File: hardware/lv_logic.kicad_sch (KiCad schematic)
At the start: 3 parts, among them IC2 CD4081BM96, IC3 CD40106BM96, IC4 CD4081BM96

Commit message: add enable timer in logic block
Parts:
- added C6: ??, symbol Device:C
- added Q4: NMOS, symbol Simulation_SPICE:NMOS
- added R6: ??, symbol Device:R_US
- added R8: 10k, symbol Device:R_US
- added U2: Inverter_Schmitt_Dual, symbol 74xGxx:Inverter_Schmitt_Dual
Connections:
- net +12V_LOGIC: now also R6.1, U2.5 (V_{CC})
- net +12V_SHDW: no longer IC2.13 (H)
- net ENABLE_IN: now also Q4.2 (G), R8.2; no longer IC2.12 (G), IC2.2 (B), IC4.1 (A)
- net GND: now also C6.2, Q4.3 (S), R8.1, U2.2 (GND), U2.3 (2A)
- new net: C6.1, Q4.1 (D), R6.2, U2.1 (1A)
- new net: IC2.12 (G), IC4.1 (A), U2.6 (1Y)
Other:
- note added: "Enable 50ms timer"
- moved on the sheet: IC2, IC3, IC4

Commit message: create hv_power hierarchical sheet; rename hi_sense ad hv_sense to meet project standards
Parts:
- removed U2: Inverter_Schmitt_Dual, symbol 74xGxx:Inverter_Schmitt_Dual
- added IC5: TC4S584F,LF, SOT-25, symbol Libary_Loader:TC4S584F,LF
- C6: value ?? -> 1uF
- R6: value ?? -> 55k
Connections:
- net +12V_LOGIC: now also C6.2, IC5.5 (VDD)
- net +12V_SHDW: now also IC2.13 (H)
- net GND: now also IC5.3 (VSS); no longer C6.2
- net at C6.1, Q4.1 (D), R6.2: now also IC5.2 (IN_A)
- net at IC2.12 (G), IC4.1 (A): now also IC2.2 (B), IC5.4 (OUT_~{X})

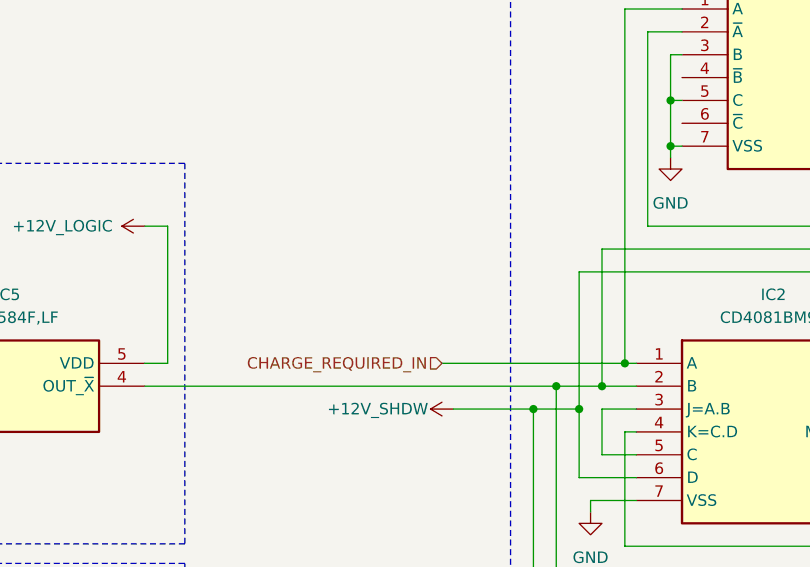
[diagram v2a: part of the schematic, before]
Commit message: refactor project layout merging high and low voltage in the same pcb
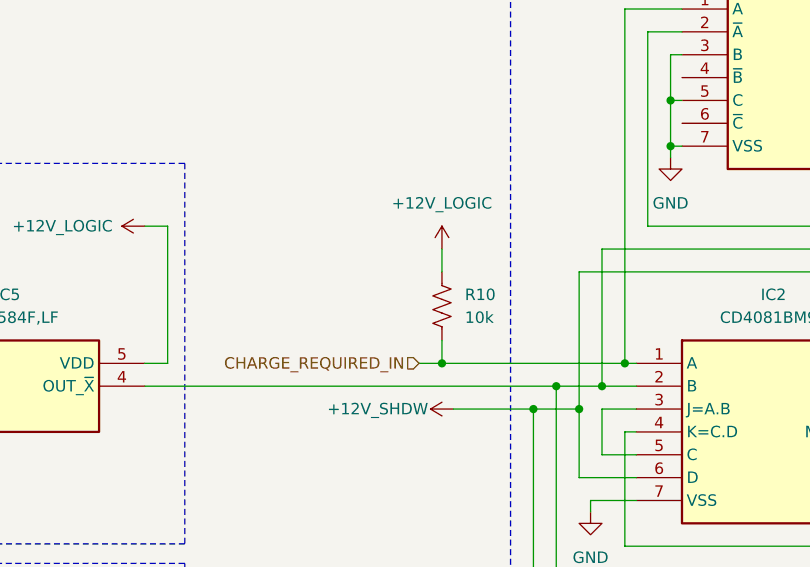
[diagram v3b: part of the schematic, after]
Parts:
- added R10: 10k, symbol Device:R_US
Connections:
- net +12V_LOGIC: now also R10.1
- net CHARGE_REQUIRED_IN: now also R10.2
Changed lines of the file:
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@@
+	)
+	(junction
+		(at 144.78 73.66)
+		(diameter 0)
+		(color 0 0 0 0)
 	)
 	(junction
@@
 	(wire
 		(pts
+			(xy 144.78 60.96) (xy 144.78 63.5)
+		)
+		(stroke
+			(width 0)
+			(type default)
+		)
+	)
+	(wire
+		(pts
 			(xy 171.45 36.83) (xy 167.64 36.83)
 		)
@@
 	(wire
 		(pts
+			(xy 144.78 71.12) (xy 144.78 73.66)
+		)
+		(stroke
+			(width 0)
+			(type default)
+		)
+	)
+	(wire
+		(pts
 			(xy 170.18 44.45) (xy 171.45 44.45)
 		)
@@
 	(wire
 		(pts
-			(xy 144.78 73.66) (xy 165.1 73.66)
-		)
-		(stroke
-			(width 0)
-			(type default)
-		)
-	)
-	(wire
-		(pts
 			(xy 196.85 76.2) (xy 214.63 76.2)
 		)
@@
 		(pts
 			(xy 111.76 73.66) (xy 114.3 73.66)
+		)
+		(stroke
+			(width 0)
+			(type default)
+		)
+	)
+	(wire
+		(pts
+			(xy 142.24 73.66) (xy 165.1 73.66)
 		)
 		(stroke
@@
 	(hierarchical_label "CHARGE_REQUIRED_IN"
 		(shape input)
-		(at 144.78 73.66 180)
+		(at 142.24 73.66 180)
 		(effects
 			(font
@@
 	)
 	(symbol
+		(lib_id "Device:R_US")
+		(at 144.78 67.31 0)
+		(unit 1)
+		(body_style 1)
+		(exclude_from_sim no)
+		(in_bom yes)
+		(on_board yes)
+		(in_pos_files yes)
+		(dnp no)
+		(fields_autoplaced yes)
+		(property "Reference" "R10"
+			(at 147.32 66.0399 0)
+			(show_name no)
+			(do_not_autoplace no)
+			(effects
+				(font
+					(size 1.27 1.27)
+				)
+				(justify left)
+			)
+		)
+		(property "Value" "10k"
+			(at 147.32 68.5799 0)
+			(show_name no)
+			(do_not_autoplace no)
+			(effects
+				(font
+					(size 1.27 1.27)
+				)
+				(justify left)
+			)
+		)
+		(property "Footprint" ""
+			(at 145.796 67.564 90)
+			(hide yes)
+			(show_name no)
+			(do_not_autoplace no)
+			(effects
+				(font
+					(size 1.27 1.27)
+				)
+			)
+		)
+		(property "Datasheet" ""
+			(at 144.78 67.31 0)
+			(hide yes)
+			(show_name no)
+			(do_not_autoplace no)
+			(effects
+				(font
+					(size 1.27 1.27)
+				)
+			)
+		)
+		(property "Description" "Resistor, US symbol"
+			(at 144.78 67.31 0)
+			(hide yes)
+			(show_name no)
+			(do_not_autoplace no)
+			(effects
+				(font
+					(size 1.27 1.27)
+				)
+			)
+		)
+		(pin "1"
+		)
+		(pin "2"
+		)
+		(instances
+			(project "precharge-controller"
+				(path "/d0dc5348-c362-4b06-85a5-76de80ed7055/56fb71d1-0eb8-422f-888e-b936ea8ae617"
+					(reference "R10")
+					(unit 1)
+				)
+			)
+		)
+	)
+	(symbol
 		(lib_id "power:GND")
 		(at 165.1 123.19 0)
@@
 					(unit 1)
 				)
+			)
+		)
+	)
+	(symbol
+		(lib_id "power:+12V")
+		(at 144.78 60.96 0)
+		(unit 1)
+		(body_style 1)
+		(exclude_from_sim no)
+		(in_bom yes)
+		(on_board yes)
+		(in_pos_files yes)
+		(dnp no)
+		(fields_autoplaced yes)
+		(property "Reference" "#PWR018"
+			(at 144.78 64.77 0)
+			(hide yes)
+			(show_name no)
+			(do_not_autoplace no)
+			(effects
+				(font
+					(size 1.27 1.27)
+				)
+			)
+		)
+		(property "Value" "+12V_LOGIC"
+			(at 144.78 55.88 0)
+			(show_name no)
+			(do_not_autoplace no)
+			(effects
+				(font
+					(size 1.27 1.27)
+				)
+			)
+		)
+		(property "Footprint" ""
+			(at 144.78 60.96 0)
+			(hide yes)
+			(show_name no)
+			(do_not_autoplace no)
+			(effects
+				(font
+					(size 1.27 1.27)
+				)
+			)
+		)
+		(property "Datasheet" ""
+			(at 144.78 60.96 0)
+			(hide yes)
+			(show_name no)
+			(do_not_autoplace no)
+			(effects
+				(font
+					(size 1.27 1.27)
+				)
+			)
+		)
+		(property "Description" "Power symbol creates a global label with name \"+12V\""
+			(at 144.78 60.96 0)
+			(hide yes)
+			(show_name no)
+			(do_not_autoplace no)
+			(effects
+				(font
+					(size 1.27 1.27)
+				)
+			)
+		)
+		(pin "1"
+		)
+		(instances
+			(project "precharge-controller"
+				(path "/d0dc5348-c362-4b06-85a5-76de80ed7055/56fb71d1-0eb8-422f-888e-b936ea8ae617"
+					(reference "#PWR018")
+					(unit 1)
+				)

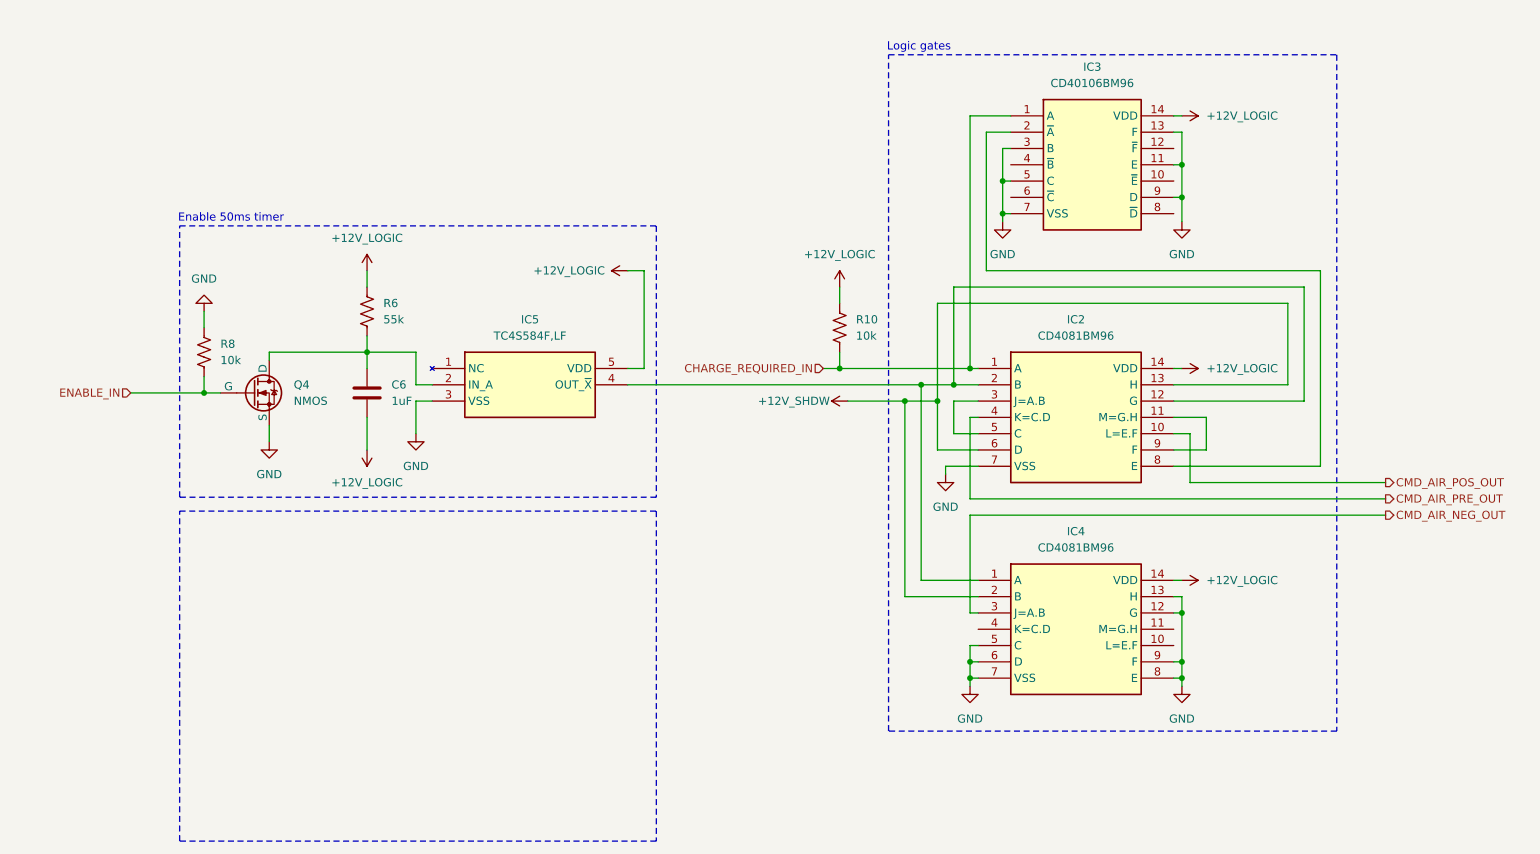
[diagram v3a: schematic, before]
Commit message: add full galvanic isoltation and comparator to hv_sense block
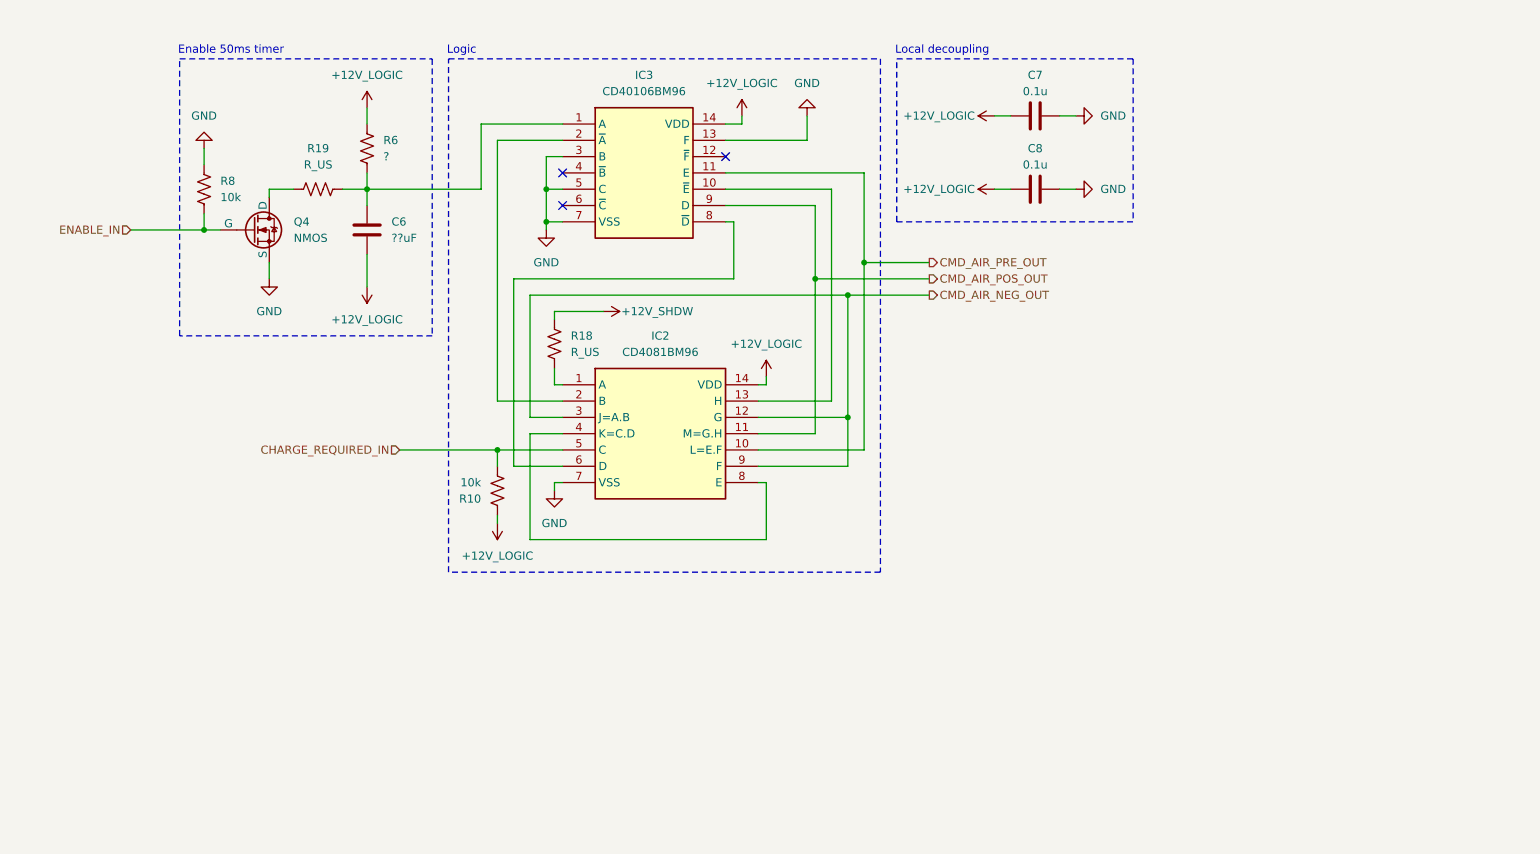
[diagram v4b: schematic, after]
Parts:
- removed IC4: CD4081BM96, SOIC127P600X175-14N, symbol Libary_Loader:CD4081BM96
- removed IC5: TC4S584F,LF, SOT-25, symbol Libary_Loader:TC4S584F,LF
- added C7, C8: 0.1u, symbol Device:C
- added R18, R19: R_US, symbol Device:R_US
- C6: value 1uF -> ??uF
- R6: value 55k -> ?
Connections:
- net +12V_LOGIC: now also C7.2, C8.2
- net +12V_SHDW: now also R18.1; no longer IC2.13 (H), IC2.6 (D)
- net CHARGE_REQUIRED_IN: now also IC2.5 (C); no longer IC2.1 (A), IC3.1 (A)
- net CMD_AIR_NEG_OUT: now also IC2.12 (G), IC2.3 (J=A.B), IC2.9 (F)
- net CMD_AIR_POS_OUT: now also IC2.11 (M=G.H), IC3.9 (D); no longer IC2.10 (L=E.F)
- net CMD_AIR_PRE_OUT: now also IC2.10 (L=E.F), IC3.11 (E); no longer IC2.4 (K=C.D)
- net GND: now also C7.1, C8.1; no longer IC3.11 (E), IC3.9 (D)
- net at C6.1, R6.2: now also IC3.1 (A), R19.2; no longer Q4.1 (D)
- net at IC2.2 (B): now also IC3.2 (~{A}); no longer IC2.12 (G)
- net at IC2.8 (E): now also IC2.4 (K=C.D); no longer IC3.2 (~{A})
- net at IC3.10 (~{E}): now also IC2.13 (H)
- net at IC3.8 (~{D}): now also IC2.6 (D)
- new net: IC2.1 (A), R18.2
- new net: Q4.1 (D), R19.1
- no-connect marks 0 -> 3
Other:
- note added: "Local decoupling"
- note added: "Logic"
- note removed: "Logic gates"
- moved on the sheet: C6, IC2, IC3, Q4, R10, R6, R8

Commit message: refactor schematic and datasheet names
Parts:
- R18, R19: value R_US -> ??
- R6: value ? -> ??
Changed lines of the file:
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@@
 			)
 		)
-		(property "Value" "R_US"
+		(property "Value" "??"
 			(at 63.5 41.91 90)
 			(show_name no)
@@
 			)
 		)
-		(property "Value" "R_US"
+		(property "Value" "??"
 			(at 102.87 71.1199 0)
 			(show_name no)
@@
 			)
 		)
-		(property "Value" "?"
+		(property "Value" "??"
 			(at 73.66 40.6399 0)
 			(show_name no)

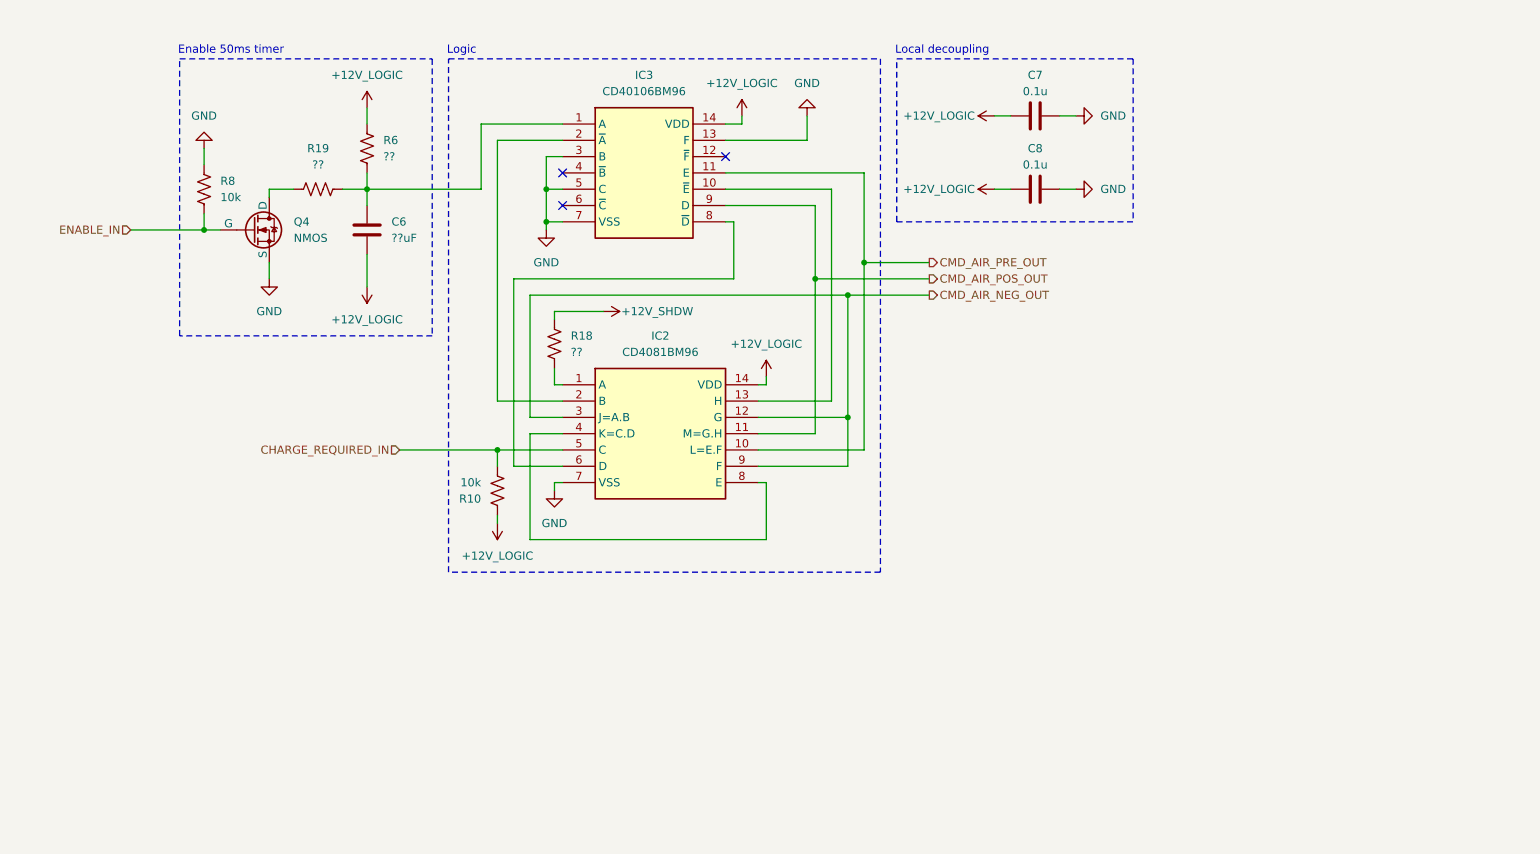
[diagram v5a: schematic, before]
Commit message: add holding voltage to lv_relay_drive block
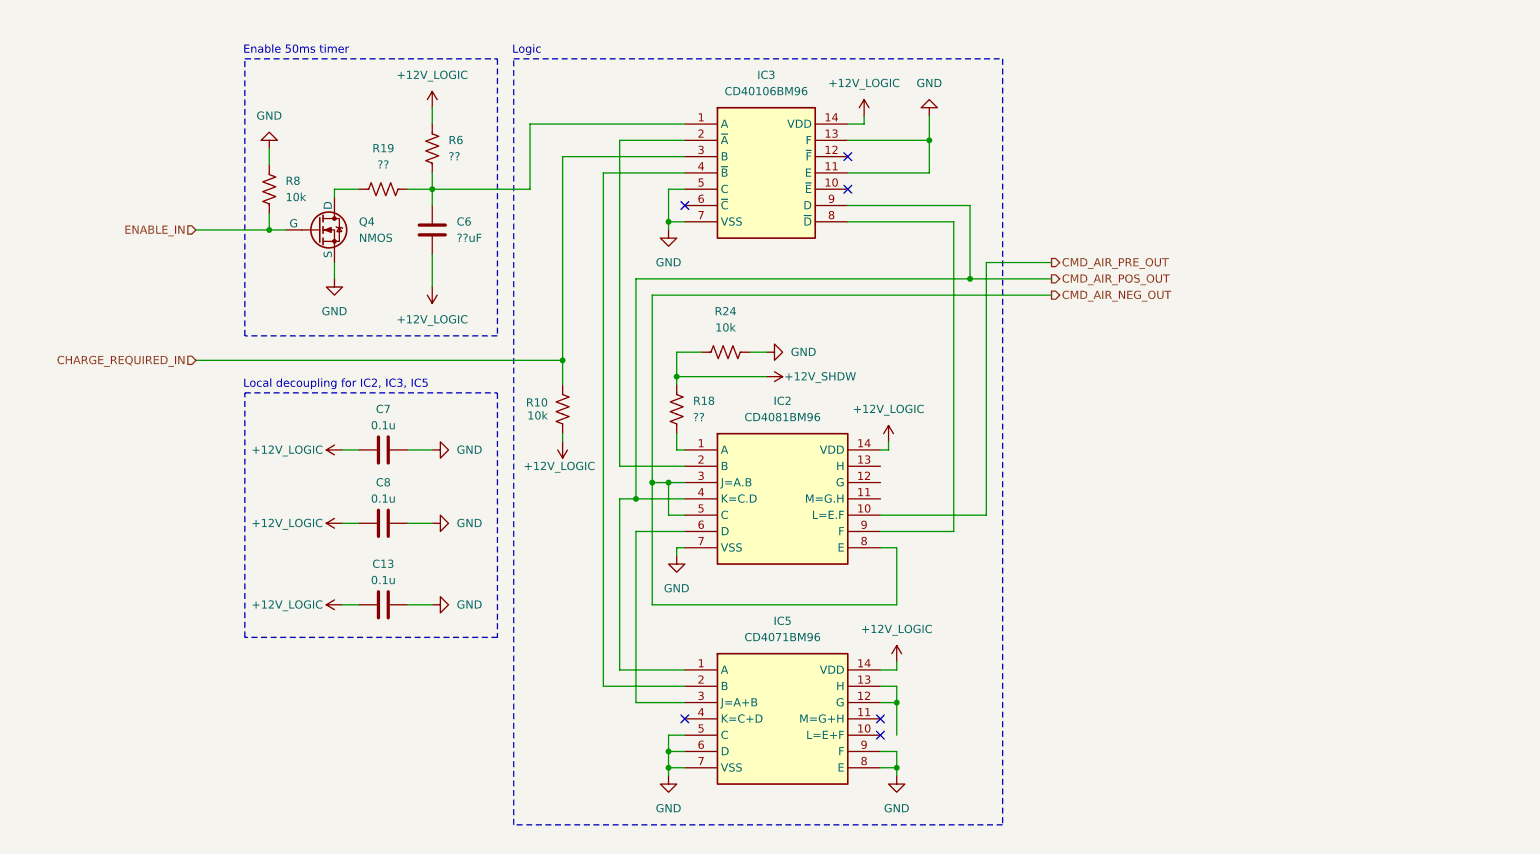
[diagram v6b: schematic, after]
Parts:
- added C13: 0.1u, symbol Device:C
- added IC5: CD4071BM96, SOIC127P600X175-14N, symbol Libary_Loader:CD4071BM96
- added R24: 10k, symbol Device:R_US
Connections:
- net +12V_LOGIC: now also C13.2, IC5.14 (VDD)
- net +12V_SHDW: now also R24.1
- net CHARGE_REQUIRED_IN: now also IC3.3 (B); no longer IC2.5 (C)
- net CMD_AIR_NEG_OUT: now also IC2.5 (C), IC2.8 (E); no longer IC2.12 (G), IC2.9 (F)
- net CMD_AIR_POS_OUT: now also IC2.4 (K=C.D), IC5.1 (A); no longer IC2.11 (M=G.H)
- net CMD_AIR_PRE_OUT: no longer IC3.11 (E)
- net GND: now also IC3.11 (E), C13.1, IC5.5 (C), IC5.6 (D), IC5.7 (VSS), IC5.8 (E), IC5.9 (F), R24.2; no longer IC3.3 (B)
- net at IC2.13 (H): no longer IC3.10 (~{E})
- net at IC2.6 (D): now also IC5.3 (J=A+B); no longer IC3.8 (~{D})
- net at IC3.4 (~{B}): now also IC5.2 (B)
- new net: IC2.9 (F), IC3.8 (~{D})
- new net: IC5.12 (G), IC5.13 (H)
- no-connect marks 3 -> 6
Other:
- note added: "Local decoupling for IC2, IC3, IC5"
- note removed: "Local decoupling"
- moved on the sheet: C6, C7, C8, IC2, IC3, Q4, R10, R18, R19, R6, R8
